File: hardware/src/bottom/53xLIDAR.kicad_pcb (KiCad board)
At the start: 2 copper layers, 75.4 x 75.4 mm, 62 parts, among them J1 CONN_01X06, J10 CONN_01X06, J11 CONN_01X06, J12 CONN_01X06, J13 CONN_01X06, J14 CONN_01X06, J15 CONN_01X06, J16 CONN_01X06, J17 USB_OTG, J18 UART_EXT, J19 I2C1_DEBUG, J2 CONN_01X06, J20 I2C2_DEBUG, J21 UART_DEBUG, J22 SWD, J23 SPI1_EXT, J25 GS3, J3 CONN_01X06, J4 CONN_01X06, J5 CONN_01X06, J6 CONN_01X06, J7 CONN_01X06, J8 CONN_01X06, J9 CONN_01X06, U1 WS2812S, U2 WS2812S, U3 WS2812S, U4 WS2812S, U5 STM32F411RETx, U6 MPU-9250, U7 KF33_DPAK, U8 LSM9DS1, Y1 24MHz SR PASSIVES 3225-24M-SR

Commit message: Bom optimization
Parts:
- C1, C12, C13, C17, C2, C20, C22, C3, C4, C5, C6, C7, C8: footprint Capacitors_SMD:C_0402 -> Capacitors_SMD:C_0603
- C14, C15, C16, C18, C19, C21, C9: footprint Capacitors_SMD:C_0805_HandSoldering -> Capacitors_SMD:C_0603_HandSoldering
- moved C12 0.29 mm to (160.6, 77.3)
- moved C13 0.27 mm to (159.0, 69.9)
- moved C1 0.25 mm to (176.7, 75.8)
- moved C14 0.25 mm to (178.1, 74.5)
- moved C7 0.25 mm to (162.6, 85.8)
- moved C3 0.23 mm to (130.4, 84.8)
- moved C4 0.14 mm to (156.0, 100.4)

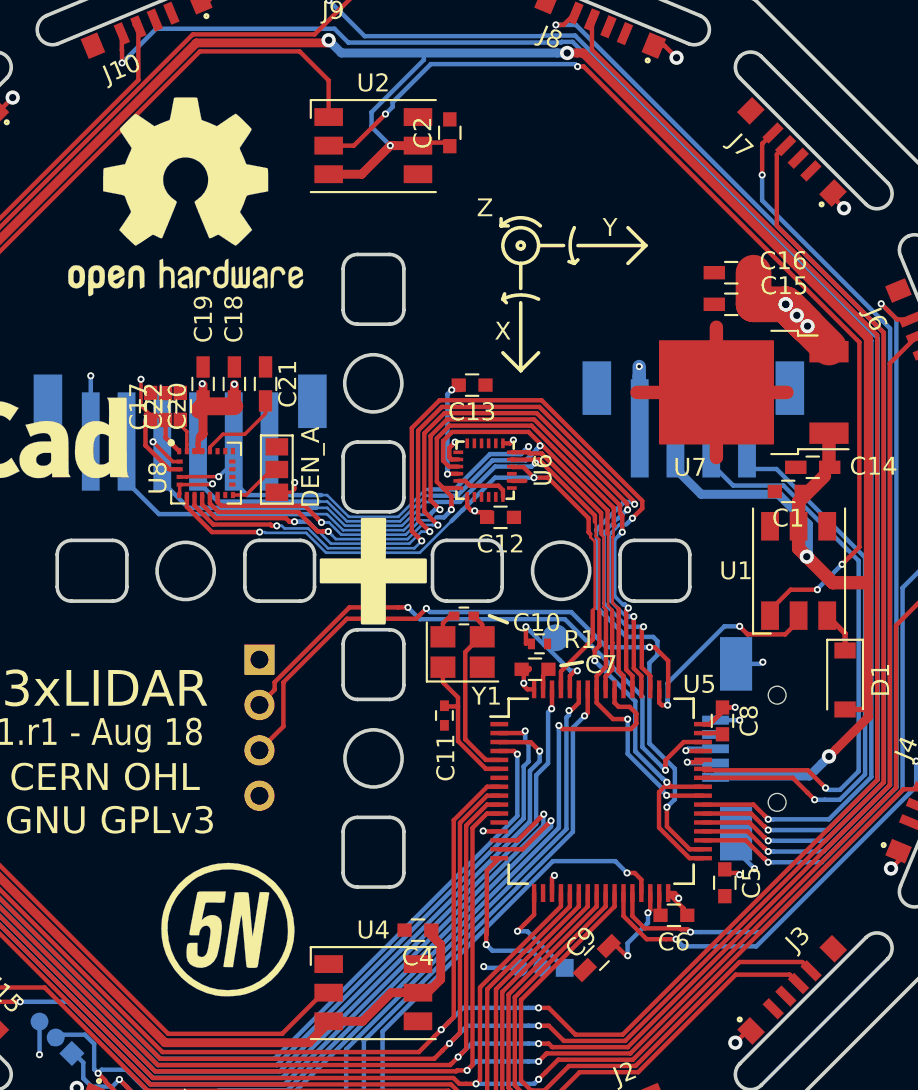
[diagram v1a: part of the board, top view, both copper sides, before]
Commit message: Fixed bugs introduced in rev1
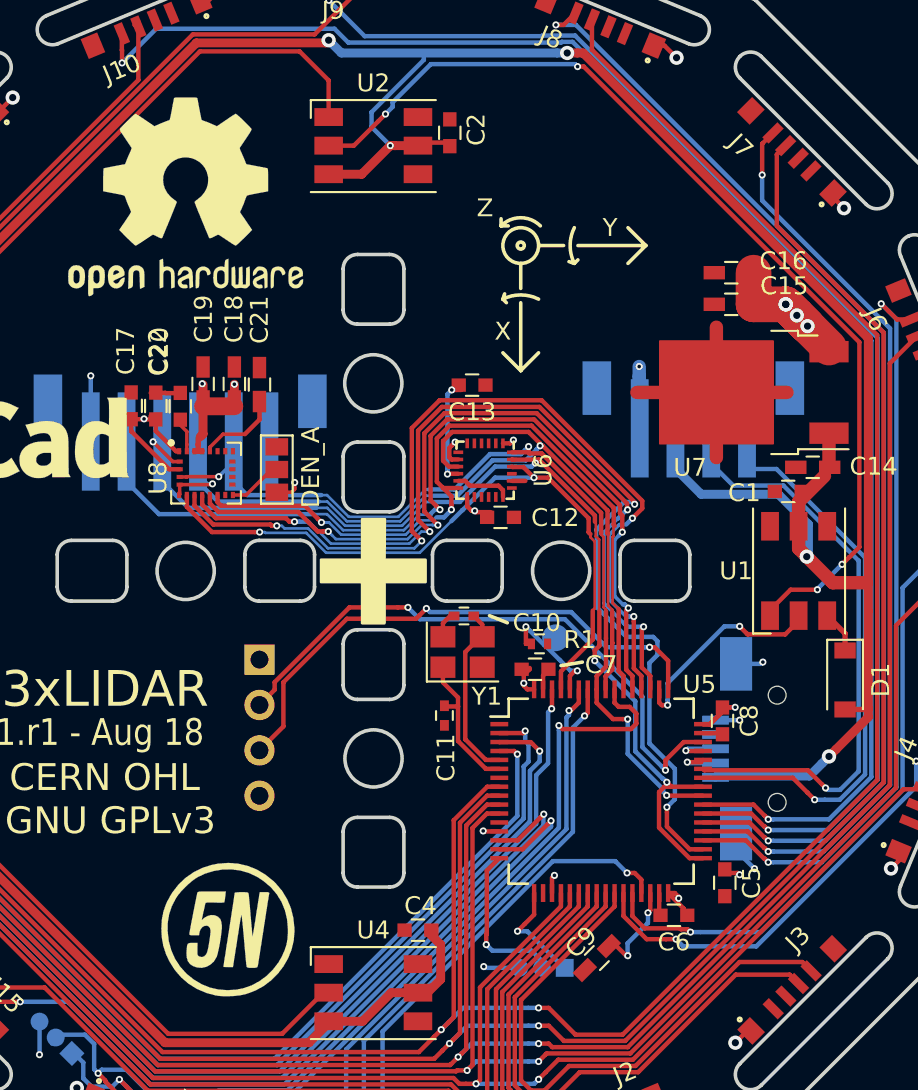
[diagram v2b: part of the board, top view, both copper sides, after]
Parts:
- moved C20 1.09 mm to (139.9, 71.1)
- moved C17 0.55 mm to (141.3, 71.1)
- moved C21 0.34 mm to (147.1, 69.9)
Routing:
- net +3V3: track 64.2 -> 62.5 mm
- net GND: track 43.4 -> 45.1 mm
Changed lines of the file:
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@@
     (thickness 1.6)
     (drawings 587)
-    (tracks 1313)
+    (tracks 1316)
     (zones 0)
     (modules 62)
@@
   )
   (module Capacitors_SMD:C_0603_HandSoldering (layer F.Cu)
-    (at 147.47 69.835 270)
+    (at 147.13 69.87 270)
     (descr "Capacitor SMD 0603, hand soldering")
     (tags "capacitor 0603")
     (attr smd)
-    (fp_text reference C21 (at 0 -1.25 270) (layer F.SilkS)
+    (fp_text reference C21 (at -3.625 0 270) (layer F.SilkS)
       (effects (font (size 1 1) (thickness 0.15)))
     )
@@
       (effects (font (size 1 1) (thickness 0.15)))
     )
-    (pad 2 smd rect (at 0.95 0 45) (size 1.2 0.75) (layers F.Cu F.Paste F.Mask)
+    (pad 2 smd rect (at 0.949999 0 45) (size 1.2 0.75) (layers F.Cu F.Paste F.Mask)
       (net 4 "Net-(C9-Pad2)"))
-    (pad 1 smd rect (at -0.95 0 45) (size 1.2 0.75) (layers F.Cu F.Paste F.Mask)
+    (pad 1 smd rect (at -0.949999 0 45) (size 1.2 0.75) (layers F.Cu F.Paste F.Mask)
       (net 1 GND))
     (model Capacitors_SMD.3dshapes/C_0603.wrl
@@
     (tags "capacitor 0603")
     (attr smd)
-    (fp_text reference C1 (at 0 -1.5 180) (layer F.SilkS)
+    (fp_text reference C1 (at 2.46 -0.08 180) (layer F.SilkS)
       (effects (font (size 1 1) (thickness 0.15)))
     )
@@
     (tags "capacitor 0603")
     (attr smd)
-    (fp_text reference C2 (at 0 -1.5 90) (layer F.SilkS)
+    (fp_text reference C2 (at 0.18 1.48 90) (layer F.SilkS)
       (effects (font (size 1 1) (thickness 0.15)))
     )
@@
     (tags "capacitor 0603")
     (attr smd)
-    (fp_text reference C4 (at 0 -1.5 180) (layer F.SilkS)
+    (fp_text reference C4 (at -0.14 1.36 180) (layer F.SilkS)
       (effects (font (size 1 1) (thickness 0.15)))
     )
@@
     (tags "capacitor 0603")
     (attr smd)
-    (fp_text reference C12 (at 0 -1.5 180) (layer F.SilkS)
+    (fp_text reference C12 (at -3.06 -0.02 180) (layer F.SilkS)
       (effects (font (size 1 1) (thickness 0.15)))
     )
@@
   )
   (module Capacitors_SMD:C_0603 (layer F.Cu)
-    (at 141.875 71.1 90)
+    (at 141.33 71.07 90)
     (descr "Capacitor SMD 0603, reflow soldering, AVX (see smccp.pdf)")
     (tags "capacitor 0603")
     (attr smd)
-    (fp_text reference C17 (at 0 -1.5 90) (layer F.SilkS)
+    (fp_text reference C17 (at 3.08 -1.685 90) (layer F.SilkS)
       (effects (font (size 1 1) (thickness 0.15)))
     )
@@
   )
   (module Capacitors_SMD:C_0603 (layer F.Cu)
-    (at 141.04 71.085 270)
+    (at 139.95 71.06 270)
     (descr "Capacitor SMD 0603, reflow soldering, AVX (see smccp.pdf)")
     (tags "capacitor 0603")
     (attr smd)
-    (fp_text reference C20 (at 0 -1.5 270) (layer F.SilkS)
+    (fp_text reference C20 (at -3.065 -1.59 270) (layer F.SilkS)
       (effects (font (size 1 1) (thickness 0.15)))
     )
@@
     (tags "capacitor 0603")
     (attr smd)
-    (fp_text reference C22 (at 0 -1.5 90) (layer F.SilkS)
+    (fp_text reference C22 (at 3.035 -1.26 90) (layer F.SilkS)
       (effects (font (size 1 1) (thickness 0.15)))
     )
@@
   (segment (start 147.71 111.24) (end 145.81 111.24) (width 0.25) (layer B.Cu) (net 1))
   (segment (start 145.81 111.24) (end 145.74 111.31) (width 0.25) (layer B.Cu) (net 1))
+  (segment (start 141.86 70.335) (end 141.875 70.35) (width 0.25) (layer F.Cu) (net 1))
+  (segment (start 141.04 70.335) (end 141.86 70.335) (width 0.25) (layer F.Cu) (net 1))
+  (segment (start 142.685 70.35) (end 142.7 70.335) (width 0.25) (layer F.Cu) (net 1))
+  (segment (start 141.875 70.35) (end 142.685 70.35) (width 0.25) (layer F.Cu) (net 1))
   (segment (start 131.4 82.5) (end 131.4 82.8) (width 0.5) (layer F.Cu) (net 2) (status 30))
   (segment (start 130.4 81.5) (end 131.4 82.5) (width 0.5) (layer F.Cu) (net 2) (status 20))
@@
   (segment (start 143.7 73.6) (end 143.495 73.6) (width 0.3) (layer F.Cu) (net 3))
   (segment (start 143.974576 71.085445) (end 145.724576 71.085445) (width 1) (layer F.Cu) (net 3))
-  (segment (start 143.775 71.285021) (end 143.974576 71.085445) (width 1) (layer F.Cu) (net 3))
-  (segment (start 141.875 72.84) (end 141.875 71.65) (width 0.25) (layer F.Cu) (net 3))
-  (segment (start 142.635 73.6) (end 141.875 72.84) (width 0.25) (layer F.Cu) (net 3))
-  (segment (start 141.86 71.635) (end 141.875 71.65) (width 0.25) (layer F.Cu) (net 3))
-  (segment (start 141.04 71.635) (end 141.86 71.635) (width 0.25) (layer F.Cu) (net 3))
   (via (at 143.925 69.825) (size 0.4) (drill 0.2) (layers F.Cu B.Cu) (net 3))
   (segment (start 143.974576 69.874576) (end 143.925 69.825) (width 0.2) (layer F.Cu) (net 3))
@@
   (segment (start 145.724576 71.085445) (end 145.724576 69.850424) (width 0.5) (layer F.Cu) (net 3))
   (segment (start 145.724576 69.850424) (end 145.725 69.85) (width 0.2) (layer F.Cu) (net 3))
-  (via (at 140.5 69.575) (size 0.4) (drill 0.2) (layers F.Cu B.Cu) (net 3))
-  (segment (start 140.5 71.045) (end 140.5 69.575) (width 0.2) (layer F.Cu) (net 3))
-  (segment (start 141.04 71.635) (end 141.04 71.585) (width 0.2) (layer F.Cu) (net 3))
-  (segment (start 141.04 71.585) (end 140.5 71.045) (width 0.2) (layer F.Cu) (net 3))
   (segment (start 143.974576 71.085445) (end 143.974576 69.874576) (width 0.5) (layer F.Cu) (net 3))
   (via (at 161.34 72.98) (size 0.4) (drill 0.2) (layers F.Cu B.Cu) (net 3))
@@
   (via (at 159.65 94.85) (size 0.4) (drill 0.2) (layers F.Cu B.Cu) (net 3))
   (segment (start 141.04 71.685) (end 141.04 71.635) (width 0.25) (layer F.Cu) (net 3))
-  (segment (start 140.75 71.975) (end 141.04 71.685) (width 0.25) (layer F.Cu) (net 3))
-  (segment (start 140.75 73.279004) (end 140.75 71.975) (width 0.25) (layer F.Cu) (net 3))
+  (segment (start 141.04 71.635) (end 141.04 71.585) (width 0.2) (layer F.Cu) (net 3))
+  (segment (start 141.33 72.47) (end 141.33 71.82) (width 0.25) (layer F.Cu) (net 3))
+  (segment (start 142.635 73.6) (end 142.46 73.6) (width 0.25) (layer F.Cu) (net 3))
+  (segment (start 142.46 73.6) (end 141.33 72.47) (width 0.25) (layer F.Cu) (net 3))
+  (segment (start 139.95 72.479004) (end 139.95 71.81) (width 0.25) (layer F.Cu) (net 3))
   (segment (start 142.665 74.61) (end 142.080996 74.61) (width 0.25) (layer F.Cu) (net 3))
-  (segment (start 142.080996 74.61) (end 140.75 73.279004) (width 0.25) (layer F.Cu) (net 3))
+  (segment (start 142.080996 74.61) (end 139.95 72.479004) (width 0.25) (layer F.Cu) (net 3))
+  (via (at 140.67 71.79) (size 0.4) (drill 0.2) (layers F.Cu B.Cu) (net 3))
+  (segment (start 141.33 71.82) (end 140.7 71.82) (width 0.25) (layer F.Cu) (net 3))
+  (segment (start 140.7 71.82) (end 140.67 71.79) (width 0.25) (layer F.Cu) (net 3))
+  (segment (start 140.65 71.81) (end 140.67 71.79) (width 0.25) (layer F.Cu) (net 3))
+  (segment (start 139.95 71.81) (end 140.65 71.81) (width 0.25) (layer F.Cu) (net 3))
   (via (at 167.74 101.83) (size 0.4) (drill 0.2) (layers F.Cu B.Cu) (net 4))
   (segment (start 167.647766 101.83) (end 166.893883 101.076117) (width 0.25) (layer F.Cu) (net 4))
@@
   (segment (start 164.536949 85.886949) (end 163.94 85.29) (width 0.25) (layer B.Cu) (net 55))
   (segment (start 163.07499 84.46) (end 162.239999 83.625009) (width 0.25) (layer B.Cu) (net 55))
-  (segment (start 162.04 83.707852) (end 162.04 83.42501) (width 0.25) (layer F.Cu) (net 55))
   (segment (start 163.11 84.46) (end 163.07499 84.46) (width 0.25) (layer B.Cu) (net 55))
-  (segment (start 162.04 84.37) (end 162.04 83.707852) (width 0.25) (layer F.Cu) (net 55))
   (segment (start 162.239999 83.625009) (end 162.04 83.42501) (width 0.25) (layer B.Cu) (net 55))
-  (segment (start 162.05 84.38) (end 162.04 84.37) (width 0.25) (layer F.Cu) (net 55))
   (via (at 162.04 83.42501) (size 0.4) (drill 0.2) (layers F.Cu B.Cu) (net 55))
-  (segment (start 147.47 71.49) (end 147.47 71.085) (width 0.2) (layer F.Cu) (net 56))
-  (segment (start 146.31 72.65) (end 147.47 71.49) (width 0.2) (layer F.Cu) (net 56))
+  (segment (start 162.05 84.38) (end 162.35 84.38) (width 0.25) (layer F.Cu) (net 55))
+  (segment (start 162.04 83.42501) (end 162.04 84.37) (width 0.25) (layer F.Cu) (net 55))
+  (segment (start 162.04 84.37) (end 162.05 84.38) (width 0.25) (layer F.Cu) (net 55))
   (segment (start 145.084998 72.65) (end 146.31 72.65) (width 0.2) (layer F.Cu) (net 56))
   (segment (start 144.35 73.384998) (end 145.084998 72.65) (width 0.2) (layer F.Cu) (net 56))
   (segment (start 144.355 73.6) (end 144.35 73.595) (width 0.2) (layer F.Cu) (net 56))
   (segment (start 144.35 73.595) (end 144.35 73.384998) (width 0.2) (layer F.Cu) (net 56))
+  (segment (start 147.13 71.83) (end 147.13 70.82) (width 0.25) (layer F.Cu) (net 56))
+  (segment (start 146.31 72.65) (end 147.13 71.83) (width 0.25) (layer F.Cu) (net 56))
   (segment (start 143.065 73.225) (end 143.065 73.6) (width 0.2) (layer F.Cu) (net 57))
   (segment (start 143.065 72.5) (end 143.065 73.225) (width 0.2) (layer F.Cu) (net 57))
@@
     (connect_pads (clearance 0.2))
     (min_thickness 0.254)
-    (fill yes (arc_segments 32) (thermal_gap 0.508) (thermal_bridge_width 0.508))
+    (fill yes (arc_segments 32) (thermal_gap 0.2) (thermal_bridge_width 0.3))
     (polygon
       (pts

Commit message: Removed IMU axes on silkscreen as they are no longer consistent with the two IMUs
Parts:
- removed REF**: AXES, custom-footprints:AXES
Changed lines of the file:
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@@
     (tracks 1316)
     (zones 0)
-    (modules 62)
+    (modules 61)
     (nets 62)
   )
@@
     (46 B.CrtYd user)
     (47 F.CrtYd user)
-    (48 B.Fab user hide)
-    (49 F.Fab user hide)
+    (48 B.Fab user)
+    (49 F.Fab user)
   )
   (setup
@@
     )
   )
-  (module custom-footprints:AXES (layer F.Cu)
-    (at 159.25 59.49)
-    (fp_text reference REF** (at 5 4.2) (layer F.SilkS) hide
-      (effects (font (size 1 1) (thickness 0.15)))
-    )
-    (fp_text value AXES (at 5.9 5.4) (layer F.Fab) hide
-      (effects (font (size 1 1) (thickness 0.15)))
-    )
-    (fp_line (start 2.5 5.8) (end 2.5 9.6) (layer F.SilkS) (width 0.2))
-    (fp_line (start 5.7 2.6) (end 9.5 2.6) (layer F.SilkS) (width 0.2))
-    (fp_line (start 1.5 8.6) (end 2.5 9.6) (layer F.SilkS) (width 0.2))
-    (fp_line (start 2.5 9.6) (end 3.5 8.6) (layer F.SilkS) (width 0.2))
-    (fp_line (start 8.5 3.6) (end 9.5 2.6) (layer F.SilkS) (width 0.2))
-    (fp_line (start 9.5 2.6) (end 8.5 1.6) (layer F.SilkS) (width 0.2))
-    (fp_circle (center 2.5 2.6) (end 3.5 2.6) (layer F.SilkS) (width 0.2))
-    (fp_circle (center 2.5 2.6) (end 2.6 2.6) (layer F.SilkS) (width 0.4))
-    (fp_arc (start 2.5 7.6) (end 3.499999 5.600001) (angle -53.13010235) (layer F.SilkS) (width 0.2))
-    (fp_arc (start 7.5 2.6) (end 5.500001 1.600001) (angle -53.13010235) (layer F.SilkS) (width 0.2))
-    (fp_arc (start 2.5 2.6) (end 3.6 1.5) (angle -90) (layer F.SilkS) (width 0.2))
-    (fp_line (start 4.9 2.6) (end 3.5 2.6) (layer F.SilkS) (width 0.2))
-    (fp_line (start 2.5 5) (end 2.5 3.6) (layer F.SilkS) (width 0.2))
-    (fp_line (start 1.5 5.6) (end 1.7 5.8) (layer F.SilkS) (width 0.2))
-    (fp_line (start 1.5 5.6) (end 1.6 5.3) (layer F.SilkS) (width 0.2))
-    (fp_line (start 5.5 3.6) (end 5.7 3.4) (layer F.SilkS) (width 0.2))
-    (fp_line (start 5.5 3.6) (end 5.2 3.5) (layer F.SilkS) (width 0.2))
-    (fp_line (start 1.4 1.5) (end 1.4 1.1) (layer F.SilkS) (width 0.2))
-    (fp_line (start 1.4 1.5) (end 1.8 1.5) (layer F.SilkS) (width 0.2))
-    (fp_text user X (at 1.5 7.4) (layer F.SilkS)
-      (effects (font (size 1 1) (thickness 0.15)))
-    )
-    (fp_text user Y (at 7.5 1.6) (layer F.SilkS)
-      (effects (font (size 1 1) (thickness 0.15)))
-    )
-    (fp_text user Z (at 0.5 0.5) (layer F.SilkS)
-      (effects (font (size 1 1) (thickness 0.15)))
-    )
-  )
